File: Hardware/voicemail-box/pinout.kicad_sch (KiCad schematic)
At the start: 5 parts, among them CN201 Conn_02x08_Odd_Even

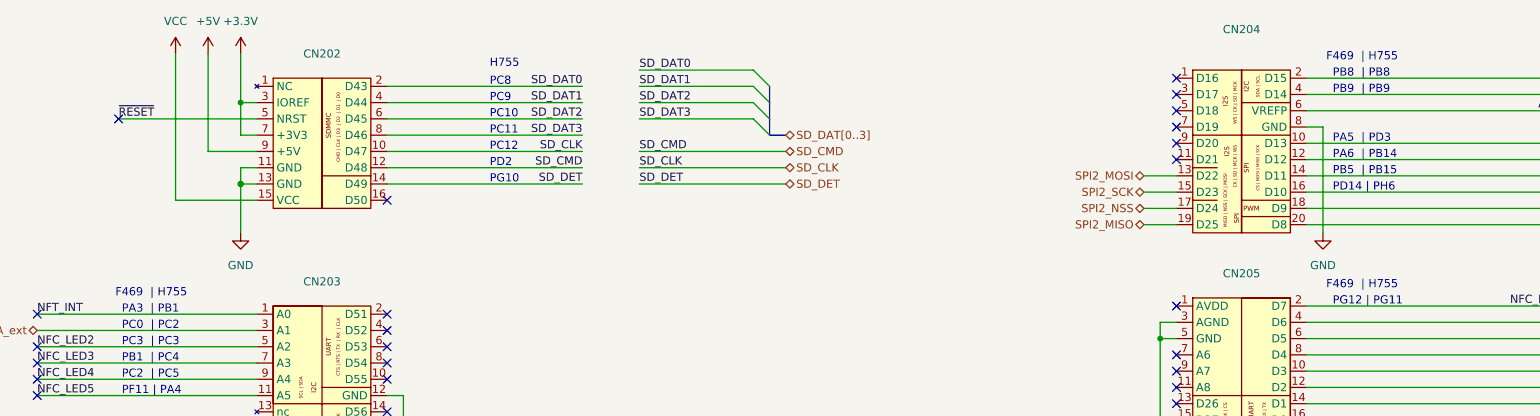
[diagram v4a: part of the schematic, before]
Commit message: corrected pinout to nucleo description
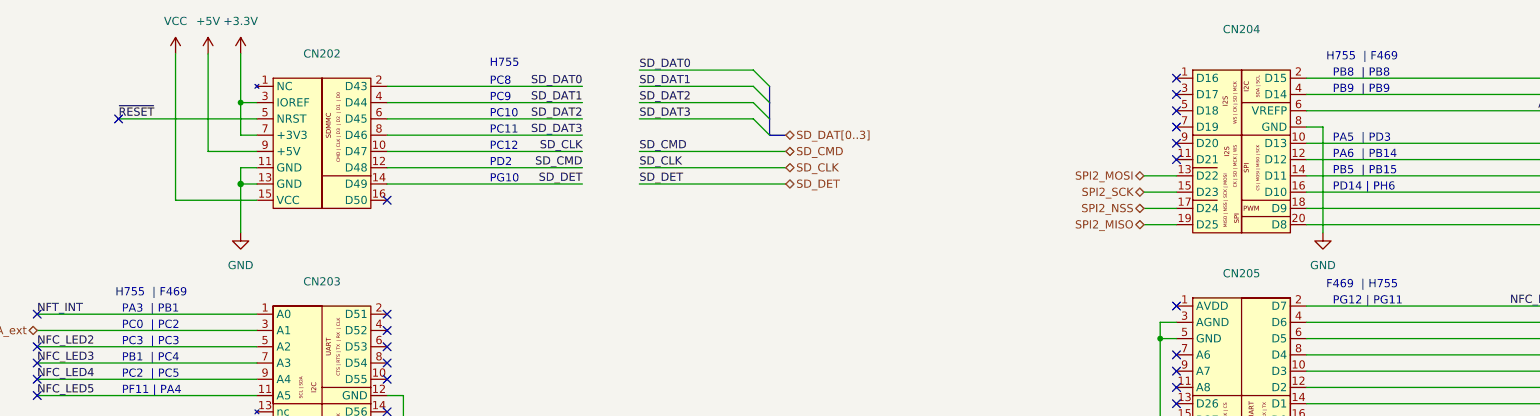
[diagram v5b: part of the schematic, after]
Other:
- note added: "H755 | F469"
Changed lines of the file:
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@@
 	(generator_version "9.0")
 	(paper "A4")
+	(text "H755  | F469"
+		(exclude_from_sim no)
+		(at 43.942 63.5 0)
+		(effects
+			(font
+				(face "Courier 10 Pitch")
+				(size 1.27 1.27)
+			)
+			(justify left bottom)
+		)
+	)
+	(text "PD2"
+		(exclude_from_sim no)
+		(at 102.362 43.18 0)
+		(effects
+			(font
+				(face "Courier 10 Pitch")
+				(size 1.27 1.27)
+			)
+			(justify left bottom)
+		)
+	)
+	(text "PB9  | PB9"
+		(exclude_from_sim no)
+		(at 233.934 31.75 0)
+		(effects
+			(font
+				(face "Courier 10 Pitch")
+				(size 1.27 1.27)
+			)
+			(justify left bottom)
+		)
+	)
+	(text "PC3  | PC3"
+		(exclude_from_sim no)
+		(at 44.958 71.12 0)
+		(effects
+			(font
+				(face "Courier 10 Pitch")
+				(size 1.27 1.27)
+			)
+			(justify left bottom)
+		)
+	)
+	(text "PC9"
+		(exclude_from_sim no)
+		(at 102.362 33.02 0)
+		(effects
+			(font
+				(face "Courier 10 Pitch")
+				(size 1.27 1.27)
+			)
+			(justify left bottom)
+		)
+	)
+	(text "PC0  | PC2"
+		(exclude_from_sim no)
+		(at 44.958 68.58 0)
+		(effects
+			(font
+				(face "Courier 10 Pitch")
+				(size 1.27 1.27)
+			)
+			(justify left bottom)
+		)
+	)
+	(text "PD14 | PH6"
+		(exclude_from_sim no)
+		(at 233.934 46.99 0)
+		(effects
+			(font
+				(face "Courier 10 Pitch")
+				(size 1.27 1.27)
+			)
+			(justify left bottom)
+		)
+	)
+	(text "PC8"
+		(exclude_from_sim no)
+		(at 102.362 30.48 0)
+		(effects
+			(font
+				(face "Courier 10 Pitch")
+				(size 1.27 1.27)
+			)
+			(justify left bottom)
+		)
+	)
+	(text "PB1  | PC4"
+		(exclude_from_sim no)
+		(at 44.958 73.66 0)
+		(effects
+			(font
+				(face "Courier 10 Pitch")
+				(size 1.27 1.27)
+			)
+			(justify left bottom)
+		)
+	)
+	(text "PA5  | PD3"
+		(exclude_from_sim no)
+		(at 233.934 39.37 0)
+		(effects
+			(font
+				(face "Courier 10 Pitch")
+				(size 1.27 1.27)
+			)
+			(justify left bottom)
+		)
+	)
+	(text "PC10"
+		(exclude_from_sim no)
+		(at 102.362 35.56 0)
+		(effects
+			(font
+				(face "Courier 10 Pitch")
+				(size 1.27 1.27)
+			)
+			(justify left bottom)
+		)
+	)
+	(text "PA3  | PB1"
+		(exclude_from_sim no)
+		(at 44.958 66.04 0)
+		(effects
+			(font
+				(face "Courier 10 Pitch")
+				(size 1.27 1.27)
+			)
+			(justify left bottom)
+		)
+	)
+	(text "Expansion Connector of:\nSTM32F469I-DISCO\n"
+		(exclude_from_sim no)
+		(at 39.37 127.762 0)
+		(effects
+			(font
+				(size 1.27 1.27)
+			)
+		)
+	)
+	(text "PC2  | PC5"
+		(exclude_from_sim no)
+		(at 44.958 76.2 0)
+		(effects
+			(font
+				(face "Courier 10 Pitch")
+				(size 1.27 1.27)
+			)
+			(justify left bottom)
+		)
+	)
+	(text "PC12"
+		(exclude_from_sim no)
+		(at 102.362 40.64 0)
+		(effects
+			(font
+				(face "Courier 10 Pitch")
+				(size 1.27 1.27)
+			)
+			(justify left bottom)
+		)
+	)
+	(text "PF11 | PA4"
+		(exclude_from_sim no)
+		(at 44.958 78.74 0)
+		(effects
+			(font
+				(face "Courier 10 Pitch")
+				(size 1.27 1.27)
+			)
+			(justify left bottom)
+		)
+	)
+	(text "PB5  | PB15"
+		(exclude_from_sim no)
+		(at 233.934 44.45 0)
+		(effects
+			(font
+				(face "Courier 10 Pitch")
+				(size 1.27 1.27)
+			)
+			(justify left bottom)
+		)
+	)
 	(text "F469  | H755"
 		(exclude_from_sim no)
-		(at 43.942 63.5 0)
-		(effects
-			(font
-				(face "Courier 10 Pitch")
-				(size 1.27 1.27)
-			)
-			(justify left bottom)
-		)
-	)
-	(text "PD2"
-		(exclude_from_sim no)
-		(at 102.362 43.18 0)
-		(effects
-			(font
-				(face "Courier 10 Pitch")
-				(size 1.27 1.27)
-			)
-			(justify left bottom)
-		)
-	)
-	(text "PB9  | PB9"
-		(exclude_from_sim no)
-		(at 233.934 31.75 0)
-		(effects
-			(font
-				(face "Courier 10 Pitch")
-				(size 1.27 1.27)
-			)
-			(justify left bottom)
-		)
-	)
-	(text "PC3  | PC3"
-		(exclude_from_sim no)
-		(at 44.958 71.12 0)
-		(effects
-			(font
-				(face "Courier 10 Pitch")
-				(size 1.27 1.27)
-			)
-			(justify left bottom)
-		)
-	)
-	(text "PC9"
-		(exclude_from_sim no)
-		(at 102.362 33.02 0)
-		(effects
-			(font
-				(face "Courier 10 Pitch")
-				(size 1.27 1.27)
-			)
-			(justify left bottom)
-		)
-	)
-	(text "PC0  | PC2"
-		(exclude_from_sim no)
-		(at 44.958 68.58 0)
-		(effects
-			(font
-				(face "Courier 10 Pitch")
-				(size 1.27 1.27)
-			)
-			(justify left bottom)
-		)
-	)
-	(text "PD14 | PH6"
-		(exclude_from_sim no)
-		(at 233.934 46.99 0)
-		(effects
-			(font
-				(face "Courier 10 Pitch")
-				(size 1.27 1.27)
-			)
-			(justify left bottom)
-		)
-	)
-	(text "PC8"
-		(exclude_from_sim no)
-		(at 102.362 30.48 0)
-		(effects
-			(font
-				(face "Courier 10 Pitch")
-				(size 1.27 1.27)
-			)
-			(justify left bottom)
-		)
-	)
-	(text "PB1  | PC4"
-		(exclude_from_sim no)
-		(at 44.958 73.66 0)
-		(effects
-			(font
-				(face "Courier 10 Pitch")
-				(size 1.27 1.27)
-			)
-			(justify left bottom)
-		)
-	)
-	(text "PA5  | PD3"
-		(exclude_from_sim no)
-		(at 233.934 39.37 0)
-		(effects
-			(font
-				(face "Courier 10 Pitch")
-				(size 1.27 1.27)
-			)
-			(justify left bottom)
-		)
-	)
-	(text "PC10"
-		(exclude_from_sim no)
-		(at 102.362 35.56 0)
-		(effects
-			(font
-				(face "Courier 10 Pitch")
-				(size 1.27 1.27)
-			)
-			(justify left bottom)
-		)
-	)
-	(text "PA3  | PB1"
-		(exclude_from_sim no)
-		(at 44.958 66.04 0)
-		(effects
-			(font
-				(face "Courier 10 Pitch")
-				(size 1.27 1.27)
-			)
-			(justify left bottom)
-		)
-	)
-	(text "Expansion Connector of:\nSTM32F469I-DISCO\n"
-		(exclude_from_sim no)
-		(at 39.37 127.762 0)
-		(effects
-			(font
-				(size 1.27 1.27)
-			)
-		)
-	)
-	(text "PC2  | PC5"
-		(exclude_from_sim no)
-		(at 44.958 76.2 0)
-		(effects
-			(font
-				(face "Courier 10 Pitch")
-				(size 1.27 1.27)
-			)
-			(justify left bottom)
-		)
-	)
-	(text "PC12"
-		(exclude_from_sim no)
-		(at 102.362 40.64 0)
-		(effects
-			(font
-				(face "Courier 10 Pitch")
-				(size 1.27 1.27)
-			)
-			(justify left bottom)
-		)
-	)
-	(text "PF11 | PA4"
-		(exclude_from_sim no)
-		(at 44.958 78.74 0)
-		(effects
-			(font
-				(face "Courier 10 Pitch")
-				(size 1.27 1.27)
-			)
-			(justify left bottom)
-		)
-	)
-	(text "PB5  | PB15"
-		(exclude_from_sim no)
-		(at 233.934 44.45 0)
-		(effects
-			(font
-				(face "Courier 10 Pitch")
-				(size 1.27 1.27)
-			)
-			(justify left bottom)
-		)
-	)
-	(text "F469  | H755"
-		(exclude_from_sim no)
 		(at 232.918 62.23 0)
 		(effects
@@
 		)
 	)
-	(text "F469  | H755"
+	(text "H755  | F469"
 		(exclude_from_sim no)
 		(at 232.918 26.67 0)

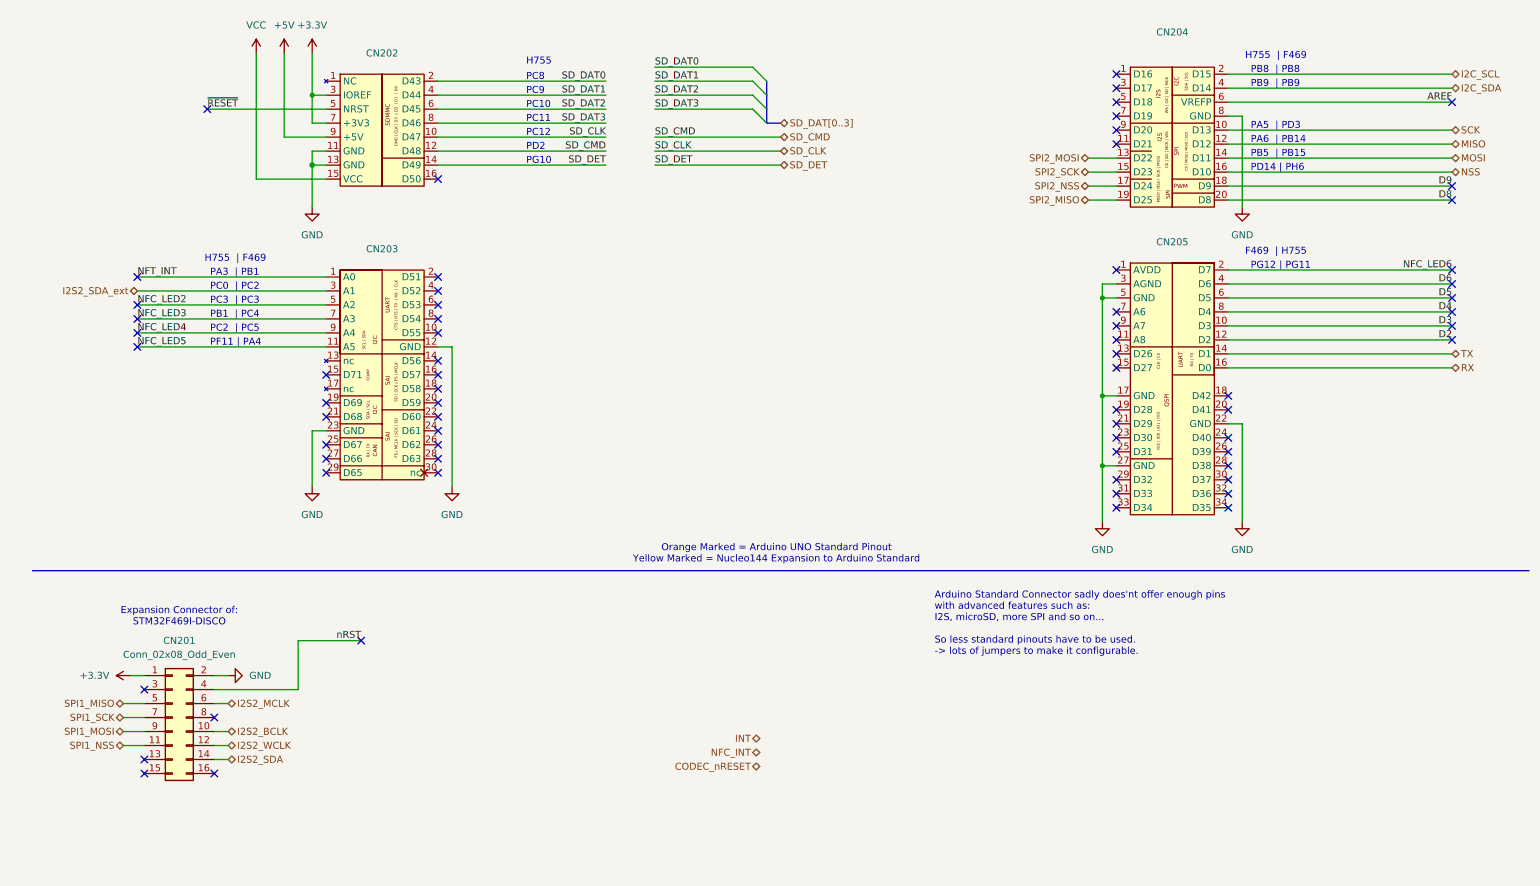
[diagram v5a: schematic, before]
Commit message: HW Layout progress todo: + Antenna + Audio Jacks + Planes (Supply only)
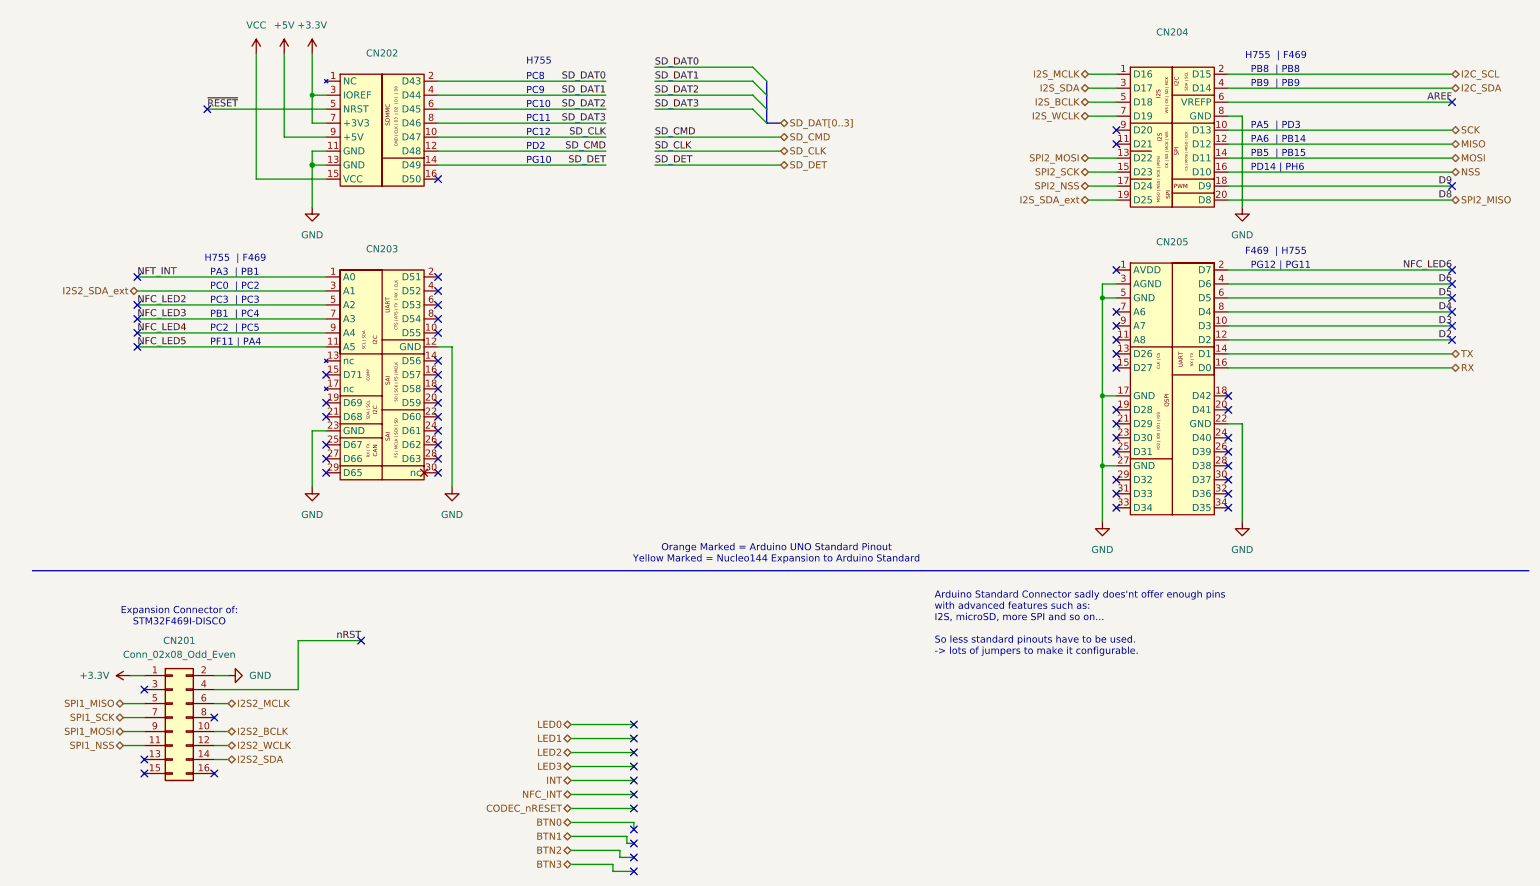
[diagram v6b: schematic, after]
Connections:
- net D8 is gone; now on net SPI2_MISO: CN204.20 (D8)
- net SPI2_MISO: no longer CN204.19 (D25)
- net I2S_MCLK: now reaches CN204.1 (D16)
- net I2S_SDA: now reaches CN204.3 (D17)
- net I2S_BCLK: now reaches CN204.5 (D18)
- net I2S_WCLK: now reaches CN204.7 (D19)
- new net I2S_SDA_ext: CN204.19 (D25)
- no-connect marks 69 -> 75

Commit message: layout progress step
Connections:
- net D2 is gone; now on net LED3: CN205.12 (D2)
- net D3 is gone; now on net BTN3: CN205.10 (D3)
- net D4 is gone; now on net LED2: CN205.8 (D4)
- net D5 is gone; now on net BTN2: CN205.6 (D5)
- net D6 is gone; now on net LED1: CN205.4 (D6)
- net D9 is gone; now on net LED0: CN204.18 (D9)
- net NFC_LED6 is gone; now on net BTN1: CN205.2 (D7)
- no-connect marks 75 -> 60
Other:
- note removed: "F469 | H755"
- note removed: "PG12 | PG11"

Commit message: schema review
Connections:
- net NFT_INT is gone; now on net NFC_INT: CN203.1 (A0)
- net BTN1: no longer CN205.2 (D7)
- net BTN2: no longer CN205.6 (D5)
- net BTN3: no longer CN205.10 (D3)
- net LED0: no longer CN204.18 (D9)
- net LED1: no longer CN205.4 (D6)
- net LED2: no longer names the net of CN205.8 (D4)
- net LED3: no longer names the net of CN205.12 (D2)
- net NFC_LED2: no longer names the net of CN203.5 (A2)
- net NFC_LED3: no longer names the net of CN203.7 (A3)
- net NFC_LED4: no longer names the net of CN203.9 (A4)
- net NFC_LED5: no longer names the net of CN203.11 (A5)
- no-connect marks 60 -> 74
